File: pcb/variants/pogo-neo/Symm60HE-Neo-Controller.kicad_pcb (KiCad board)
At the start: 2 copper layers, 57 x 28 mm, 38 parts, among them J1 TYPE-C-31-M-12, J2 FFC_12P, J3 FFC_12P, SW1 TS-1187A, SW2 TS-1187A, U1 AT32F405RCT7, U2 USBLC6-2SC6, U3 TLV75733PDBV, U4 XC6206P332MR, Y1 12MHz

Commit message: Controller 57 x 27 mm straight rear edge; FPC jumpers into ZIF connectors; Neo Ergo mounting topology
Extend the former local J1 setback across the complete rear edge of the FFC
daughterboard and the Neo controller so the HRO USB-C shell projects 1.0 mm
beyond one straight wall; no component or trace moves. Regenerate all
fabrication releases, panels, Fusion references and renders for the 57 x 27 mm
outline; all twelve DRC reports are clean.

Re-specify the four board interconnects as custom 12-conductor FPC jumpers
with 0.3 mm reinforced same-side tails into the BOOMELE C20111 ZIF connectors
(length TBD from the case route) and update the BOM, READMEs and generators
accordingly. Document that the spring-head modules follow the Neo Ergo
daughterboard mounting topology.

Strip 642 macOS AppleDouble files, rebuild the four JLCPCB and pogo16 Gerber
ZIPs they had been swept into, recompute those checksum lists, and make
release.py and release_pogo16.py skip ._* and .DS_Store like the Neo
generators already do.

Co-Authored-By: Claude Opus 5 <noreply@anthropic.com>
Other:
- board size 57 x 28 mm -> 57 x 27 mm
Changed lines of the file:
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@@
 		)
 		(embedded_fonts no)
-		(model "${SYMM60HE_3DMODEL_DIR}/USB_C_Receptacle_HRO_TYPE-C-31-M-12.STEP"
-			(offset
-				(xyz 0 0 0)
-			)
-			(scale
-				(xyz 1 1 1)
-			)
-			(rotate
-				(xyz 0 0 0)
-			)
-		)
 	)
 	(footprint "Symm60HE_Project:C148_C_0603_1608Metric"
@@
 	)
 	(gr_line
-		(start 154.709 -6.7633)
+		(start 154.709 -5.7633)
 		(end 154.709 19.2367)
 		(stroke
@@
 	)
 	(gr_line
-		(start 154.7138 -6.8613)
-		(end 154.709 -6.7633)
+		(start 154.7138 -5.8613)
+		(end 154.709 -5.7633)
 		(stroke
 			(width 0.1)
@@
 	)
 	(gr_line
-		(start 154.7282 -6.9584)
-		(end 154.7138 -6.8613)
+		(start 154.7282 -5.9584)
+		(end 154.7138 -5.8613)
 		(stroke
 			(width 0.1)
@@
 	)
 	(gr_line
-		(start 154.7521 -7.0535)
-		(end 154.7282 -6.9584)
+		(start 154.7521 -6.0535)
+		(end 154.7282 -5.9584)
 		(stroke
 			(width 0.1)
@@
 	)
 	(gr_line
-		(start 154.7851 -7.1459)
-		(end 154.7521 -7.0535)
+		(start 154.7851 -6.1459)
+		(end 154.7521 -6.0535)
 		(stroke
 			(width 0.1)
@@
 	)
 	(gr_line
-		(start 154.8271 -7.2347)
-		(end 154.7851 -7.1459)
+		(start 154.8271 -6.2347)
+		(end 154.7851 -6.1459)
 		(stroke
 			(width 0.1)
@@
 	)
 	(gr_line
-		(start 154.8775 -7.3188)
-		(end 154.8271 -7.2347)
+		(start 154.8775 -6.3188)
+		(end 154.8271 -6.2347)
 		(stroke
 			(width 0.1)
@@
 	)
 	(gr_line
-		(start 154.936 -7.3977)
-		(end 154.8775 -7.3188)
+		(start 154.936 -6.3977)
+		(end 154.8775 -6.3188)
 		(stroke
 			(width 0.1)
@@
 	)
 	(gr_line
-		(start 155.0019 -7.4704)
-		(end 154.936 -7.3977)
+		(start 155.0019 -6.4704)
+		(end 154.936 -6.3977)
 		(stroke
 			(width 0.1)
@@
 	)
 	(gr_line
-		(start 155.0746 -7.5363)
-		(end 155.0019 -7.4704)
+		(start 155.0746 -6.5363)
+		(end 155.0019 -6.4704)
 		(stroke
 			(width 0.1)
@@
 	)
 	(gr_line
-		(start 155.1534 -7.5947)
-		(end 155.0746 -7.5363)
+		(start 155.1534 -6.5947)
+		(end 155.0746 -6.5363)
 		(stroke
 			(width 0.1)
@@
 	)
 	(gr_line
-		(start 155.2376 -7.6452)
-		(end 155.1534 -7.5947)
+		(start 155.2376 -6.6452)
+		(end 155.1534 -6.5947)
 		(stroke
 			(width 0.1)
@@
 	)
 	(gr_line
-		(start 155.3263 -7.6871)
-		(end 155.2376 -7.6452)
+		(start 155.3263 -6.6871)
+		(end 155.2376 -6.6452)
 		(stroke
 			(width 0.1)
@@
 	)
 	(gr_line
-		(start 155.4187 -7.7202)
-		(end 155.3263 -7.6871)
+		(start 155.4187 -6.7202)
+		(end 155.3263 -6.6871)
 		(stroke
 			(width 0.1)
@@
 	)
 	(gr_line
-		(start 155.5139 -7.744)
-		(end 155.4187 -7.7202)
+		(start 155.5139 -6.744)
+		(end 155.4187 -6.7202)
 		(stroke
 			(width 0.1)
@@
 	)
 	(gr_line
-		(start 155.611 -7.7584)
-		(end 155.5139 -7.744)
+		(start 155.611 -6.7584)
+		(end 155.5139 -6.744)
 		(stroke
 			(width 0.1)
@@
 	)
 	(gr_line
-		(start 155.709 -7.7633)
-		(end 155.611 -7.7584)
+		(start 155.709 -6.7633)
+		(end 155.611 -6.7584)
 		(stroke
 			(width 0.1)
@@
 	)
 	(gr_line
-		(start 185.209 -7.7633)
-		(end 155.709 -7.7633)
-		(stroke
-			(width 0.1)
-			(type solid)
-		)
-		(layer "Edge.Cuts")
-	)
-	(gr_line
-		(start 185.709 -7.2633)
-		(end 185.209 -7.7633)
-		(stroke
-			(width 0.1)
-			(type solid)
-		)
-		(layer "Edge.Cuts")
-	)
-	(gr_line
-		(start 185.709 -6.7633)
-		(end 185.709 -7.2633)
-		(stroke
-			(width 0.1)
-			(type solid)
-		)
-		(layer "Edge.Cuts")
-	)
-	(gr_line
-		(start 198.709 -7.2633)
-		(end 198.709 -6.7633)
-		(stroke
-			(width 0.1)
-			(type solid)
-		)
-		(layer "Edge.Cuts")
-	)
-	(gr_line
-		(start 198.709 -6.7633)
-		(end 185.709 -6.7633)
-		(stroke
-			(width 0.1)
-			(type solid)
-		)
-		(layer "Edge.Cuts")
-	)
-	(gr_line
-		(start 199.209 -7.7633)
-		(end 198.709 -7.2633)
-		(stroke
-			(width 0.1)
-			(type solid)
-		)
-		(layer "Edge.Cuts")
-	)
-	(gr_line
-		(start 210.709 -7.7633)
-		(end 199.209 -7.7633)
+		(start 210.709 -6.7633)
+		(end 155.709 -6.7633)
 		(stroke
 			(width 0.1)
@@
 	)
 	(gr_line
-		(start 210.807 -7.7584)
-		(end 210.709 -7.7633)
+		(start 210.807 -6.7584)
+		(end 210.709 -6.7633)
 		(stroke
 			(width 0.1)
@@
 	)
 	(gr_line
-		(start 210.9041 -7.744)
-		(end 210.807 -7.7584)
+		(start 210.9041 -6.744)
+		(end 210.807 -6.7584)
 		(stroke
 			(width 0.1)
@@
 	)
 	(gr_line
-		(start 210.9993 -7.7202)
-		(end 210.9041 -7.744)
+		(start 210.9993 -6.7202)
+		(end 210.9041 -6.744)
 		(stroke
 			(width 0.1)
@@
 	)
 	(gr_line
-		(start 211.0917 -7.6871)
-		(end 210.9993 -7.7202)
+		(start 211.0917 -6.6871)
+		(end 210.9993 -6.7202)
 		(stroke
 			(width 0.1)
@@
 	)
 	(gr_line
-		(start 211.1804 -7.6452)
-		(end 211.0917 -7.6871)
+		(start 211.1804 -6.6452)
+		(end 211.0917 -6.6871)
 		(stroke
 			(width 0.1)
@@
 	)
 	(gr_line
-		(start 211.2646 -7.5947)
-		(end 211.1804 -7.6452)
+		(start 211.2646 -6.5947)
+		(end 211.1804 -6.6452)
 		(stroke
 			(width 0.1)
@@
 	)
 	(gr_line
-		(start 211.3434 -7.5363)
-		(end 211.2646 -7.5947)
+		(start 211.3434 -6.5363)
+		(end 211.2646 -6.5947)
 		(stroke
 			(width 0.1)
@@
 	)
 	(gr_line
-		(start 211.4161 -7.4704)
-		(end 211.3434 -7.5363)
+		(start 211.4161 -6.4704)
+		(end 211.3434 -6.5363)
 		(stroke
 			(width 0.1)
@@
 	)
 	(gr_line
-		(start 211.482 -7.3977)
-		(end 211.4161 -7.4704)
+		(start 211.482 -6.3977)
+		(end 211.4161 -6.4704)
 		(stroke
 			(width 0.1)
@@
 	)
 	(gr_line
-		(start 211.5405 -7.3188)
-		(end 211.482 -7.3977)
+		(start 211.5405 -6.3188)
+		(end 211.482 -6.3977)
 		(stroke
 			(width 0.1)
@@
 	)
 	(gr_line
-		(start 211.5909 -7.2347)
-		(end 211.5405 -7.3188)
+		(start 211.5909 -6.2347)
+		(end 211.5405 -6.3188)
 		(stroke
 			(width 0.1)
@@
 	)
 	(gr_line
-		(start 211.6329 -7.1459)
-		(end 211.5909 -7.2347)
+		(start 211.6329 -6.1459)
+		(end 211.5909 -6.2347)
 		(stroke
 			(width 0.1)
@@
 	)
 	(gr_line
-		(start 211.6659 -7.0535)
-		(end 211.6329 -7.1459)
+		(start 211.6659 -6.0535)
+		(end 211.6329 -6.1459)
 		(stroke
 			(width 0.1)
@@
 	)
 	(gr_line
-		(start 211.6898 -6.9584)
-		(end 211.6659 -7.0535)
+		(start 211.6898 -5.9584)
+		(end 211.6659 -6.0535)
 		(stroke
 			(width 0.1)
@@
 	)
 	(gr_line
-		(start 211.7042 -6.8613)
-		(end 211.6898 -6.9584)
+		(start 211.7042 -5.8613)
+		(end 211.6898 -5.9584)
 		(stroke
 			(width 0.1)
@@
 	)
 	(gr_line
-		(start 211.709 -6.7633)
-		(end 211.7042 -6.8613)
+		(start 211.709 -5.7633)
+		(end 211.7042 -5.8613)
 		(stroke
 			(width 0.1)
@@
 	(gr_line
 		(start 211.709 19.2367)
-		(end 211.709 -6.7633)
+		(end 211.709 -5.7633)
 		(stroke
 			(width 0.1)

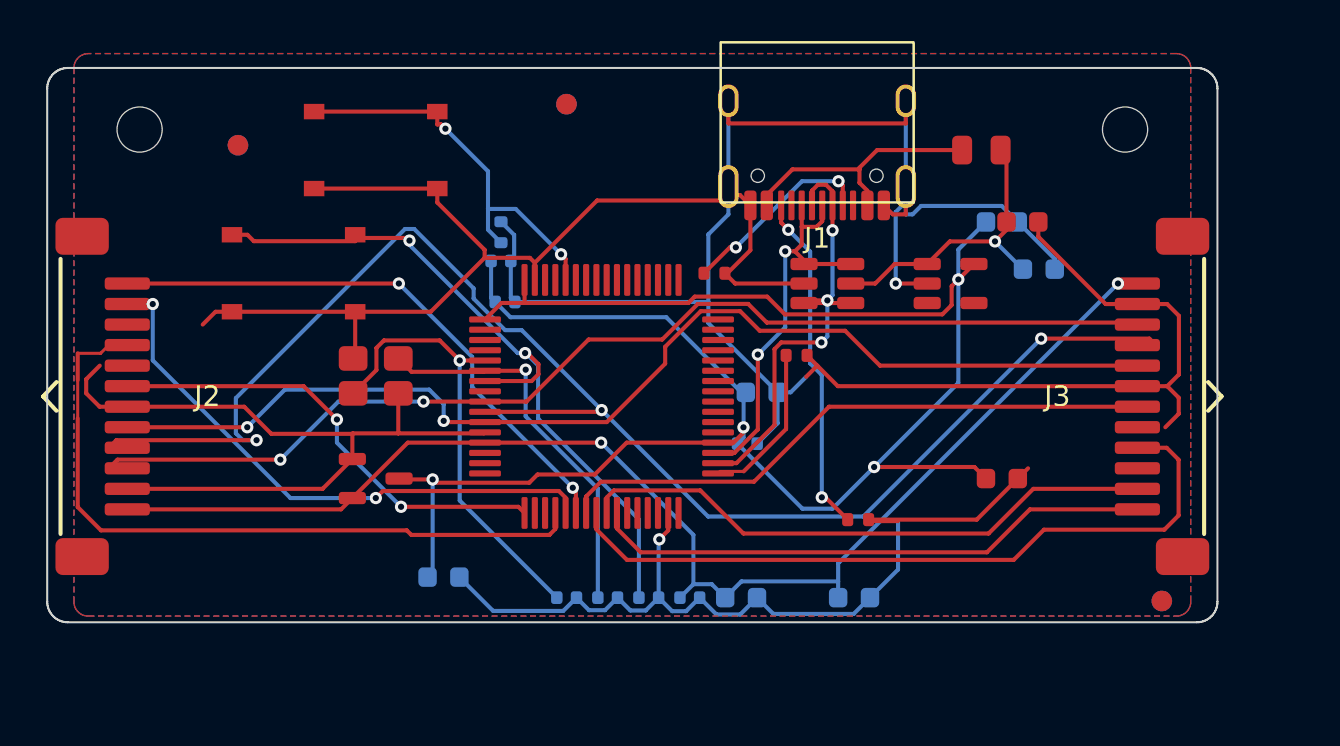
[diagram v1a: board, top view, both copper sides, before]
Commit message: Replace the project with the reorganised T7 tree: ribbon keyboard is production, pogo archived
Production design is now the outward-facing FPC keyboard with per-key
SK6812MINI-E reverse-mount LEDs, a fifth SN74LV4051A mux per half so every
alternate Hall position has its own channel, an SN74AHCT1G125 LED level
shifter, a 50 x 31 mm daughterboard, 1.5 mm POM plates and 3 degree / 7 degree
tent and typing angles. The universal half panel is fully populated (359
placements) with routed NPTH alignment slots for the mutually exclusive
positions, and eight fixed-layout Left/Right PCB pairs are released under
release/layout-pcbs/ with matching BOM, CPL, Gerber ZIP, drill report and DRC.

Reorganise tools/ into cad/, generators/, layouts/, pcb/, pogo/, releases/ and
rendering/ subpackages; add designs/ and layout/ (KLE) trees and per-layout
gallery renders. The Fusion handoff is a fourteen-body reference STEP with
Gateron KS-20 switch and Cherry-profile keycap references and exact BOOMELE,
HRO and XKB models under case/fusion360/models/official/ with provenance.

The Neo-style pogo variant, its Mill-Max vendor models, the Fusion setup
script and the pogo release packages are archived as design history and
marked DO-NOT-ORDER. Their restored BOM snapshots had reintroduced the wrong
mux part C7792; corrected to C128414 / SN74LV4051ADR and their checksum lists
and archives rebuilt.

Co-Authored-By: Claude Opus 5 <noreply@anthropic.com>
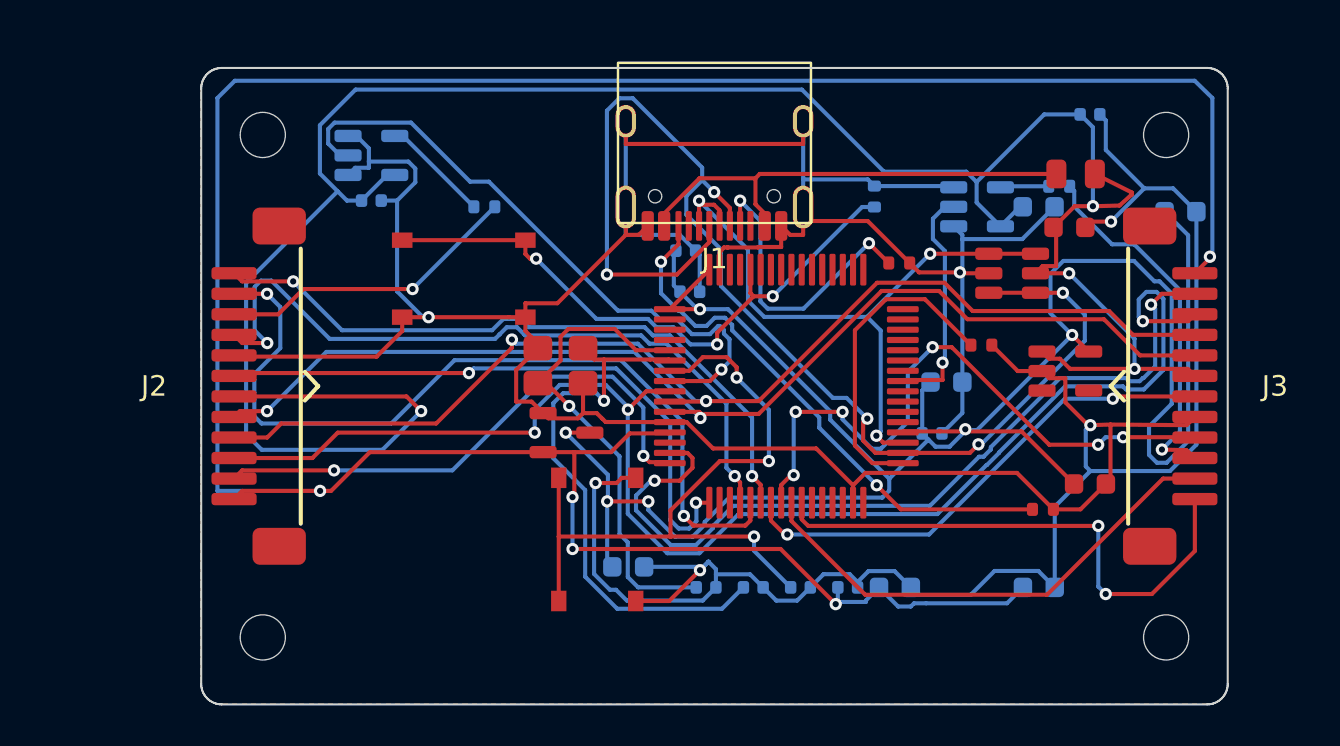
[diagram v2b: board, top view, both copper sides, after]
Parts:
- removed FIDB1, FIDB2, FIDB3: FIDUCIAL_1MM_BCU, Symm60HE_Project:Fiducial_1mm_BCu
- removed FIDF1, FIDF2, FIDF3: FIDUCIAL_1MM_FCU, Symm60HE_Project:Fiducial_1mm_FCu
- added C16: 100n, Symm60HE_Project:C1_C_0402_1005Metric, B.Cu at (170.5, -0.30)
- added C17: 100n, Symm60HE_Project:C1_C_0402_1005Metric, B.Cu at (205.5, -4.50)
- added MHD3: M2_NPTH, Symm60HE_Project:MountingHole_2.2mm_M2_NPTH, F.Cu at (209.2, -3.50)
- added MHD4: M2_NPTH, Symm60HE_Project:MountingHole_2.2mm_M2_NPTH, F.Cu at (165.2, 21.0)
- added R5: 470R, Symm60HE_Project:R3_R_0402_1005Metric, B.Cu at (176.0, 0.00)
- added R6: 470R, Symm60HE_Project:R3_R_0402_1005Metric, B.Cu at (204.0, -1.00)
- added U5: SN74AHCT1G125, Symm60HE_Project:U2_SOT-23-5, B.Cu at (170.5, -2.50)
- added U6: SN74AHCT1G125, Symm60HE_Project:U2_SOT-23-5, B.Cu at (200.0, 0.00)
- moved MHD2 24.8 mm to (209.2, 21.0)
- moved SW2 19.7 mm to (181.5, 16.2), turned to 90 degrees
- moved R4 18.3 mm to (195.0, -0.50)
- moved U4 9.56 mm to (180.0, 11.0)
- moved C14 9.01 mm to (183.0, 17.5)
- moved C15 9.01 mm to (203.0, 18.5)
- moved C5 9.01 mm to (186.0, 4.14)
- moved C6 9.01 mm to (197.8, 11.0)
- moved C7 9.01 mm to (185.8, 2.14)
- moved C8 9.01 mm to (198.5, 8.54)
- moved R1 9.01 mm to (200.2, 6.74)
- moved R2 9.01 mm to (196.2, 2.74)
- moved R3 9.01 mm to (203.2, 14.7)
- moved U1 9.01 mm to (190.7, 8.74)
- moved U2 9.01 mm to (201.7, 3.24)
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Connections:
- J2 pad 1: ADC_L4 -> +3V3A
- J2 pad 10: MUX_A0 -> RGB_L
- J2 pad 11: GND -> ADC_L3
- J2 pad 12: +3V3A -> ADC_L4
- J2 pad 2: ADC_L3 -> ADC_L5
- J2 pad 3: GND -> MUX_A0
- J2 pad 4: ADC_L2 -> MUX_A1
- J2 pad 5: GND -> MUX_A2
- J2 pad 6: ADC_L1 -> VBUS
- J2 pad 7: GND -> ADC_L1
- J2 pad 8: MUX_A2 -> GND
- J2 pad 9: MUX_A1 -> ADC_L2
- J3 pad 1: ADC_R4 -> +3V3A
- J3 pad 10: MUX_A0 -> RGB_R
- J3 pad 11: GND -> ADC_R3
- J3 pad 12: +3V3A -> ADC_R4
- J3 pad 2: ADC_R3 -> ADC_R5
- J3 pad 3: GND -> MUX_A0
- J3 pad 4: ADC_R2 -> MUX_A1
- J3 pad 5: GND -> MUX_A2
- J3 pad 6: ADC_R1 -> VBUS
- J3 pad 7: GND -> ADC_R1
- J3 pad 8: MUX_A2 -> GND
- J3 pad 9: MUX_A1 -> ADC_R2
- U1 pad 15: (no net) -> ADC_R5
- U1 pad 16: (no net) -> ADC_L5
- U1 pad 41: (no net) -> RGB_R_MCU
- U1 pad 8: (no net) -> RGB_L_MCU
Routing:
- net VBUS: track 14.6 -> 114.8 mm, vias 1 -> 4
- net +3V3A: track 65.4 -> 134.5 mm, vias 2 -> 5
- net ADC_R5: track 0.00 -> 41.0 mm, vias 0 -> 2
- net USB_DM: track 22.7 -> 60.9 mm, vias 3 -> 5
- net RGB_L_MCU: track 0.00 -> 30.8 mm, vias 0 -> 1
- net ADC_L5: track 0.00 -> 26.4 mm, vias 0 -> 2
- net MUX_A1: track 74.0 -> 55.5 mm, vias 3 -> 2
- net RGB_R: track 0.00 -> 17.8 mm, vias 0 -> 1
- net RGB_L: track 0.00 -> 14.9 mm, vias 0 -> 1
- net MUX_A0: track 54.7 -> 68.9 mm, vias 2 -> 3
- net USB_DP: track 19.4 -> 32.1 mm, vias 2 -> 3
- net ADC_L3: track 28.8 -> 40.9 mm
- net RGB_R_MCU: track 0.00 -> 11.4 mm, vias 0 -> 1
- net BOOT0: track 19.6 -> 30.0 mm, vias 2 -> 3
- net VBUS_IN: track 12.9 -> 23.0 mm
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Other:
- board size 57 x 27 mm -> 50 x 31 mm
